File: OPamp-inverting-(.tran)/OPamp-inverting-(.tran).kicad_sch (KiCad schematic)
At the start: 6 parts, among them U1 LM741

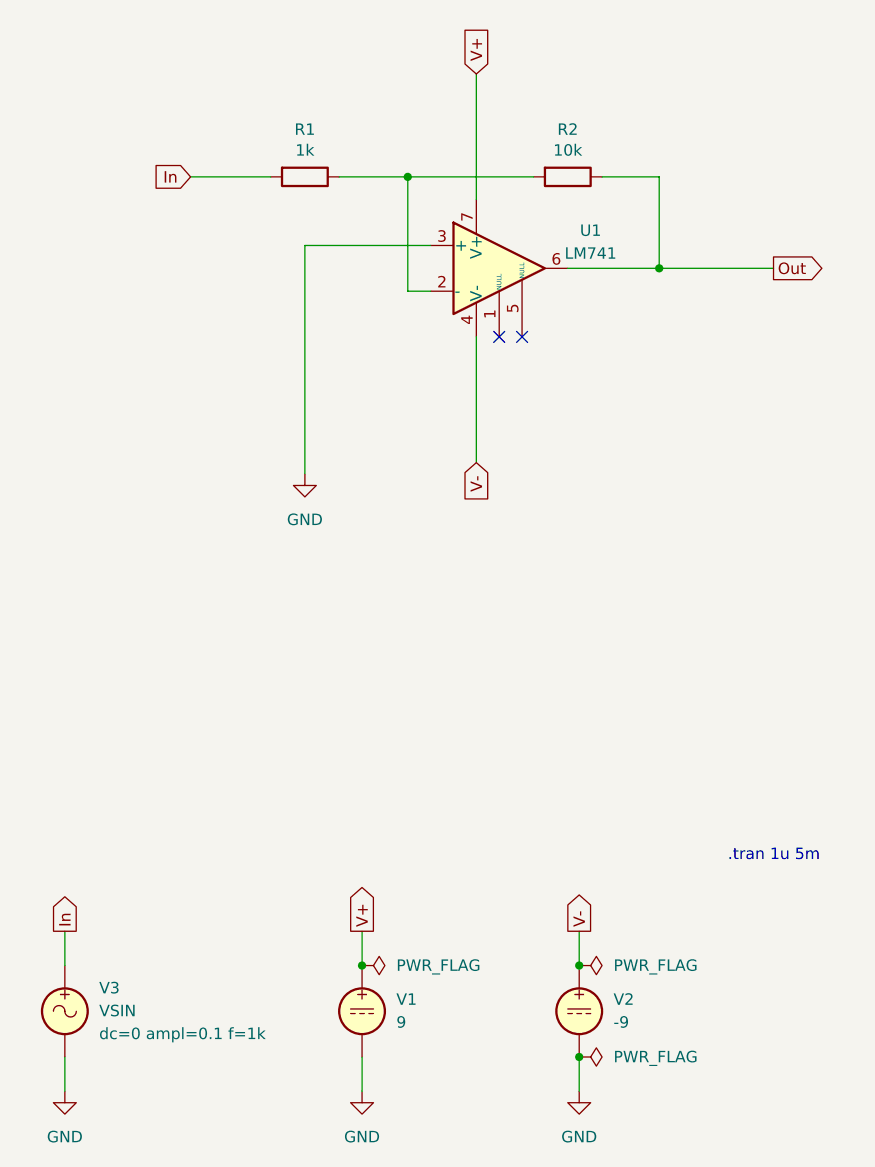
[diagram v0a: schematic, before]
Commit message: Updated all schematics and prepared for KiCad 8.0
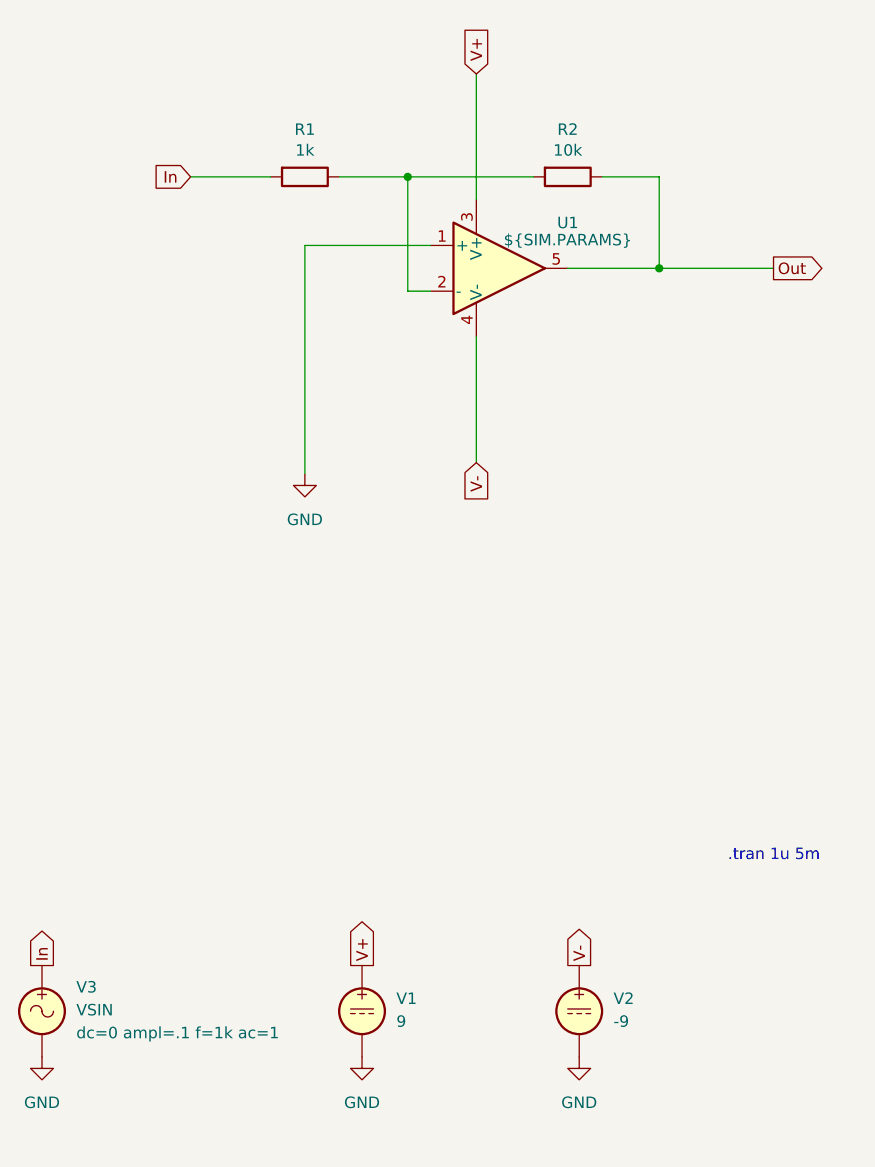
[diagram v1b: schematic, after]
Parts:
- removed U1: LM741, symbol Amplifier_Operational:LM741
- added U1: ${SIM.PARAMS}, symbol Simulation_SPICE:OPAMP
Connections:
- net GND: now also U1.1 (+)
- net Out: now also U1.5
- net V+: now also U1.3 (V+)
- net V-: now also U1.4 (V-)
- net at R1.1, R2.2: now also U1.2 (-)
- no-connect marks 2 -> 0
